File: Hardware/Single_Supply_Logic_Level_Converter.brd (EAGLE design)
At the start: 27.9 x 27.9 mm, 74 parts, among them U1 TXB0104, U2 TPS61200, U3 ADJ

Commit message: Updated per QC review
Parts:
- R1: value 200k -> (none); device SparkFun-Resistors:0603 -> SparkFun-Resistors:AXIAL-0.3
- R2: value 1.8M -> 22k
- R3: value 1k -> 13k
- R4: value 13k -> 1k
- R5: value 22k -> 1.8M
- R6: value (none) -> 200k; device SparkFun-Resistors:AXIAL-0.3 -> SparkFun-Resistors:0603
- moved R2 18.1 mm to (14.0, 1.27)
- moved R1 17.4 mm to (14.0, 1.27), turned to 180 degrees
- moved R5 15.7 mm to (19.4, 17.3)
- moved R6 14.9 mm to (16.0, 17.3), turned to 0 degrees
- moved R3 11.3 mm to (8.29, 5.00), turned to 270 degrees
- moved R4 11.3 mm to (19.5, 5.00), turned to 90 degrees
- moved C3 1.27 mm to (18.9, 21.0)
- moved L1 1.27 mm to (12.0, 25.4)
- moved U$18 1.27 mm to (21.7, 19.1)
- moved U$46 1.27 mm to (19.4, 17.0)
- moved C1 1.27 mm to (9.37, 15.2)
- moved C2 1.27 mm to (18.6, 15.2)
- moved LOGO2 1.27 mm to (14.5, 6.97)
- moved U$31 1.27 mm to (2.46, 6.35)
- moved U$41 1.27 mm to (5.05, 6.35)
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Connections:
- net 5V: now also R5.2; no longer R2.2
- net FB: now also R5.1, R6.2; no longer R1.2, R2.1
- net GND: now also R2.1, R6.1; no longer R1.1, R5.1
- net N$11: now also R1.P$1, R2.2, R3.1; no longer R4.1, R5.2, R6.P$1
- net N$3: now also R4.1; no longer R3.1
- net VCCA: now also R1.P$2; no longer R6.P$2

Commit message: adding PROD ID prefix to 1.8M
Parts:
- moved LOGO2 0.53 mm to (13.9, 7.00)
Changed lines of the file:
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@@
 <attribute name="PROD_ID" value="CAP-00810" x="24.60625" y="-8.89" size="1.778" layer="27" display="off"/>
 </element>
-<element name="LOGO2" library="SparkFun-Aesthetics" package="OSHW-LOGO-S" value="OSHW-LOGOS" x="14.478" y="6.9723" rot="MR0"/>
+<element name="LOGO2" library="SparkFun-Aesthetics" package="OSHW-LOGO-S" value="OSHW-LOGOS" x="13.9446" y="6.9977" rot="MR0"/>
 <element name="C2" library="SparkFun-Capacitors" package="0603-CAP" value="0.1uF" x="18.57375" y="15.24" rot="R180">
 <attribute name="PROD_ID" value="CAP-00810" x="-0.47625" y="39.37" size="1.778" layer="27" rot="R180" display="off"/>
@@
 </element>
 <element name="R5" library="SparkFun-Resistors" package="0603" value="1.8M" x="19.3675" y="17.30375">
-<attribute name="PROD_ID" value="13994" x="19.3675" y="17.30375" size="1.778" layer="27" display="off"/>
+<attribute name="PROD_ID" value="RES-13994" x="19.3675" y="17.30375" size="1.778" layer="27" display="off"/>
 </element>
 <element name="JP3" library="SparkFun-Connectors" package="1X04" value="455-1750-1-ND" x="26.67" y="24.13" rot="R270">

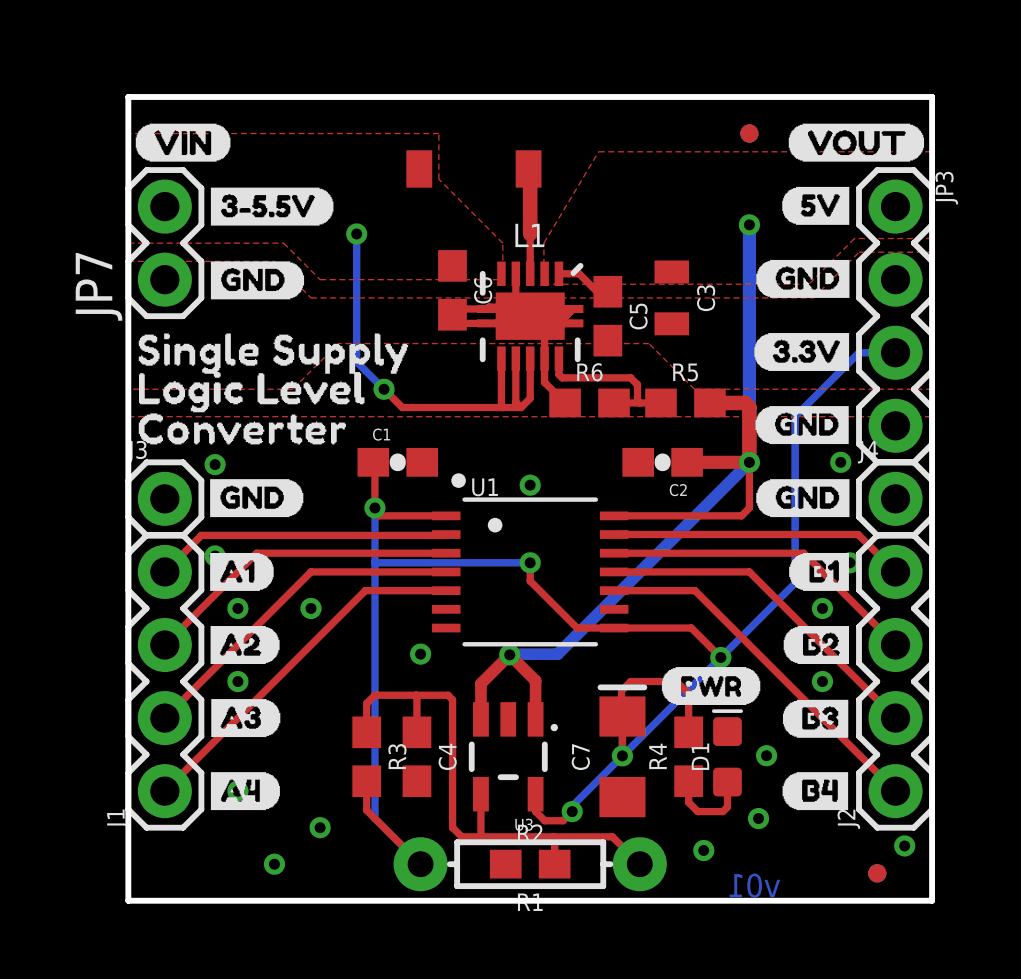
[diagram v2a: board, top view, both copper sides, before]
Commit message: Updated pin labels to SparkX standards
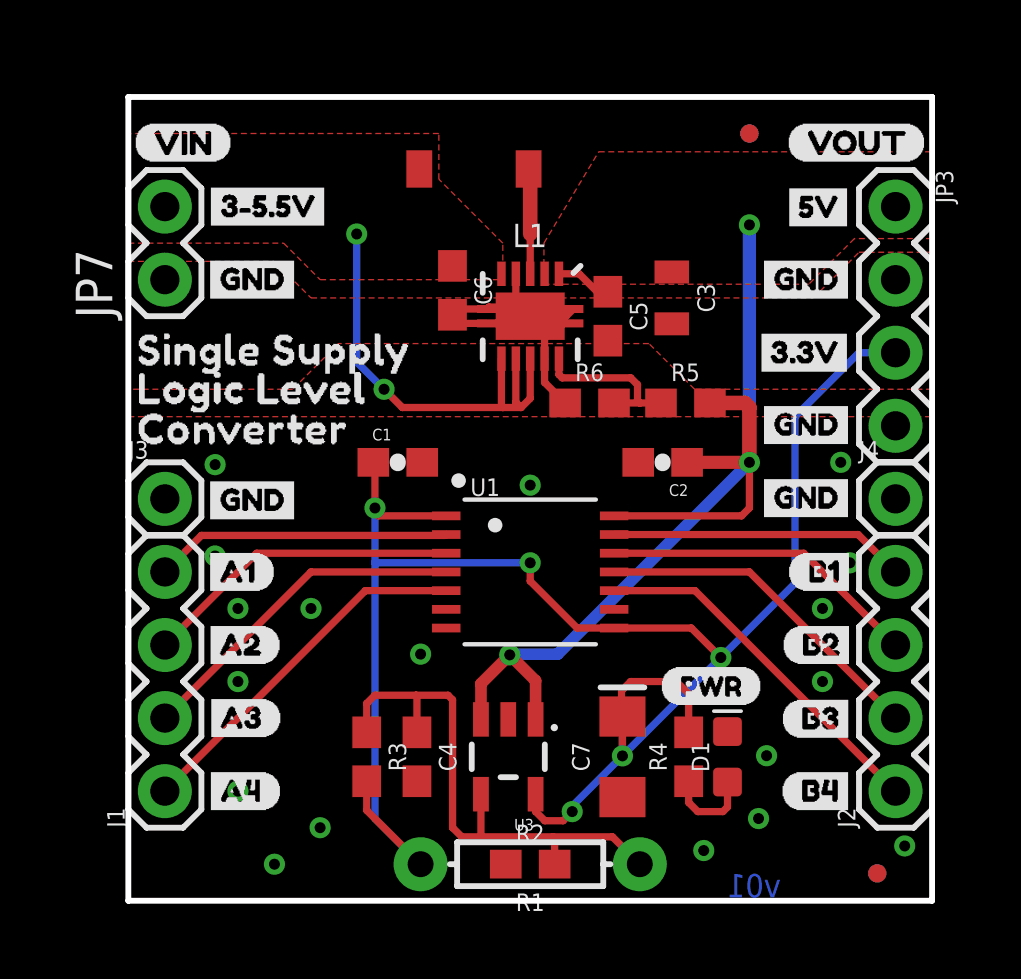
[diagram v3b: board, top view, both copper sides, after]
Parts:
- removed U$36: (no value), buzzard_labels (46):B43
- removed U$38: (no value), buzzard_labels (38):GND3
- removed U$40: (no value), buzzard_labels (38):GND0
- removed U$61: (no value), buzzard_labels (43):B34
- added U$20, U$48: (no value), buzzard_labels (51):3#3V0
- added U$21: (no value), buzzard_labels (51):3#5#5V1
- added U$23, U$47: (no value), buzzard_labels (51):5V3
- added U$44: (no value), buzzard_labels (51):GND2
- U$13, U$24: device buzzard_labels (38):GND3 -> buzzard_labels (51):GND2
- U$14, U$22, U$39, U$9: device buzzard_labels (38):GND0 -> buzzard_labels (51):GND2
- U$15: device buzzard_labels (38):GND3 -> buzzard_labels (43):B13
- U$16: device buzzard_labels (43):3#3V2 -> buzzard_labels (46):B21
- U$17: device buzzard_labels (43):3#5#5V6 -> buzzard_labels (43):B34
- U$18: device buzzard_labels (38):3#3V4 -> buzzard_labels (51):GND2
- U$19: device buzzard_labels (38):5V2 -> buzzard_labels (51):GND2
- U$25: device buzzard_labels (38):GND3 -> buzzard_labels (51):3#5#5V1
- U$33: device buzzard_labels (43):5V10 -> buzzard_labels (46):B43
- U$7: device buzzard_labels (38):3#5#5V1 -> buzzard_labels (51):GND2
- moved U$17 26.0 mm to (25.8, 6.35)
- moved U$9 23.3 mm to (25.8, 21.6), flipped to the bottom
- moved U$15 22.4 mm to (25.8, 11.4)
- moved U$33 20.3 mm to (25.8, 3.81)
- moved U$39 19.6 mm to (5.84, 14.0)
- moved U$24 19.3 mm to (2.46, 13.9)
- moved U$22 19.3 mm to (21.7, 14.0)
- moved U$25 16.7 mm to (6.86, 24.1), flipped to the bottom
- moved U$16 10.2 mm to (25.8, 8.89)
- moved U$19 7.67 mm to (21.7, 16.5)
- moved U$14 7.63 mm to (25.8, 14.0)
- moved U$18 4.85 mm to (25.8, 16.5), flipped to the bottom
- moved U$7 4.21 mm to (5.84, 21.6), flipped to the bottom
- moved U$13 0.06 mm to (21.7, 21.6)

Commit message: increased labels size
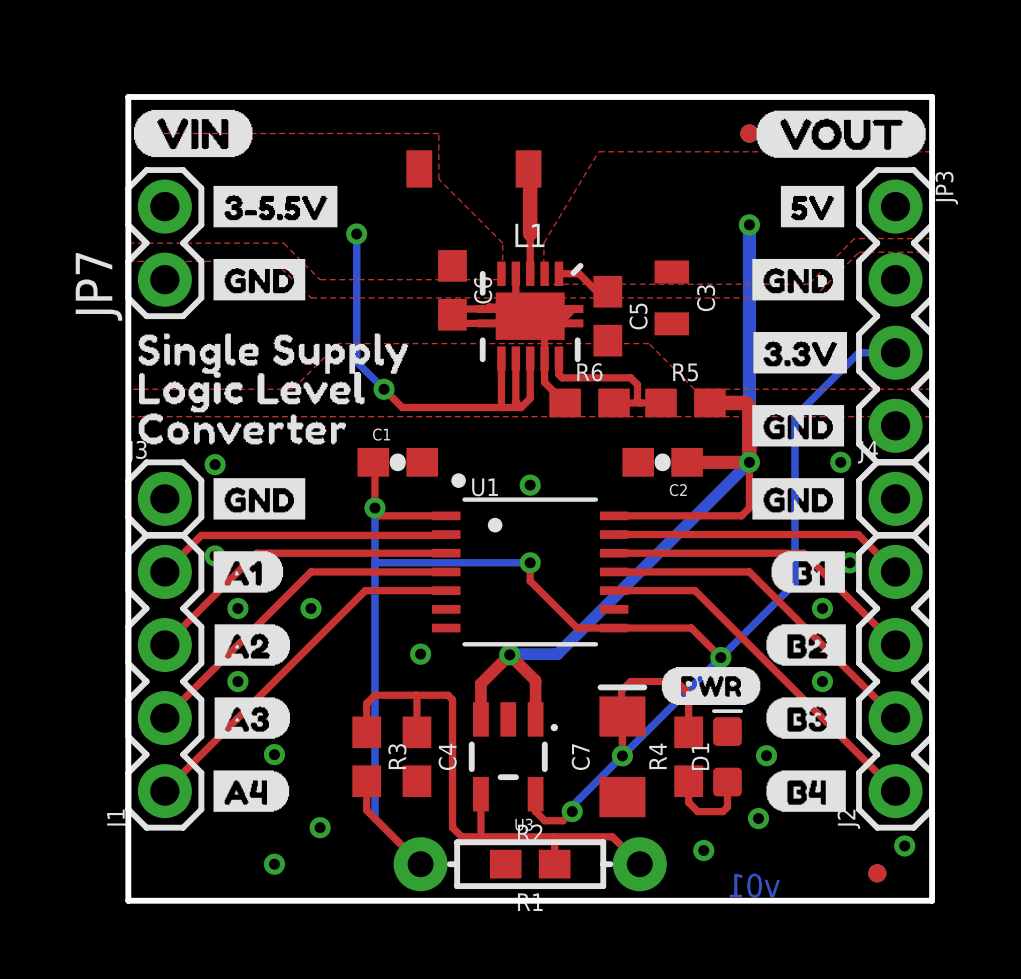
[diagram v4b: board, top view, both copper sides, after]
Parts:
- removed U$37: (no value), buzzard_labels (46):B21
- removed U$44: (no value), buzzard_labels (51):GND2
- removed U$47: (no value), buzzard_labels (51):5V3
- removed U$48: (no value), buzzard_labels (51):3#3V0
- removed U$56: (no value), buzzard_labels (38):B311
- removed U$57: (no value), buzzard_labels (38):B412
- removed U$59: (no value), buzzard_labels (43):B13
- removed U$8: (no value), Single_Supply_Logic_Level_Converter_Lables:VIN1
- added U$36, U$38: (no value), buzzard_labels (84):VIN0
- added U$40: (no value), buzzard_labels (83):GND0
- added U$51: (no value), buzzard_labels (83):5V1
- added U$53: (no value), buzzard_labels (83):3#3V2
- U$13: device buzzard_labels (51):GND2 -> buzzard_labels (83):B1_12
- U$14: device buzzard_labels (51):GND2 -> buzzard_labels (85):A21
- U$15: device buzzard_labels (43):B13 -> buzzard_labels (85):A32
- U$16: device buzzard_labels (46):B21 -> buzzard_labels (85):A43
- U$17: device buzzard_labels (43):B34 -> buzzard_labels (85):B14
- U$18: device buzzard_labels (51):GND2 -> buzzard_labels (85):B25
- U$19: device buzzard_labels (51):GND2 -> buzzard_labels (83):B2_11
- U$20: device buzzard_labels (51):3#3V0 -> buzzard_labels (83):B3_10
- U$21: device buzzard_labels (51):3#5#5V1 -> buzzard_labels (83):3#5#5V3
- U$22: device buzzard_labels (51):GND2 -> buzzard_labels (83):B4_9
- U$23: device buzzard_labels (51):5V3 -> buzzard_labels (83):3#3V2
- U$24, U$7: device buzzard_labels (51):GND2 -> buzzard_labels (83):GND0
- U$25: device buzzard_labels (51):3#5#5V1 -> buzzard_labels (83):A14
- U$26: device buzzard_labels (38):A15 -> buzzard_labels (83):A28
- U$27: device Single_Supply_Logic_Level_Converter_Lables:VIN1 -> buzzard_labels (84):VOUT1
- U$28: device Single_Supply_Logic_Level_Converter_Lables:VOUT2 -> buzzard_labels (83):A35
- U$30: device buzzard_labels (38):A26 -> buzzard_labels (83):A46
- U$31: device buzzard_labels (38):A37 -> buzzard_labels (83):GND0
- U$32: device buzzard_labels (38):A48 -> buzzard_labels (83):5V1
- U$33: device buzzard_labels (46):B43 -> buzzard_labels (85):B36
- U$34: device buzzard_labels (49):A10 -> buzzard_labels (83):GND0
- U$35: device buzzard_labels (49):A21 -> buzzard_labels (83):GND0
- U$39: device buzzard_labels (51):GND2 -> buzzard_labels (83):3#5#5V3
- U$41: device buzzard_labels (49):A32 -> buzzard_labels (83):GND0
- U$42: device buzzard_labels (49):A43 -> buzzard_labels (85):B47
- U$52: device Single_Supply_Logic_Level_Converter_Lables:VOUT2 -> buzzard_labels (83):GND0
- U$54: device buzzard_labels (38):B19 -> buzzard_labels (83):GND0
- U$55: device buzzard_labels (38):B210 -> buzzard_labels (83):GND0
- U$9: device buzzard_labels (51):GND2 -> buzzard_labels (85):A10
- moved U$28 28.5 mm to (2.54, 6.35)
- moved U$32 28.3 mm to (22.2, 24.1)
- moved U$31 24.2 mm to (21.3, 21.6)
- moved U$9 22.6 mm to (5.59, 11.4)
- moved U$27 21.6 mm to (21.7, 26.6)
- moved U$16 20.6 mm to (5.79, 3.84)
- moved U$15 20.6 mm to (5.85, 6.35)
- moved U$14 20.6 mm to (5.85, 8.90)
- moved U$42 20.4 mm to (25.4, 3.81)
- moved U$35 17.9 mm to (21.3, 16.5), flipped to the top
- moved U$34 16.6 mm to (21.3, 14.0), flipped to the top
- moved U$25 13.4 mm to (2.54, 11.4), flipped to the top
- moved U$20 12.7 mm to (22.1, 6.35)
- moved U$39 10.3 mm to (7.68, 24.1)
- moved U$22 10.2 mm to (22.1, 3.81)
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
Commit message: Decreased board width, moved R1/R2 resistors
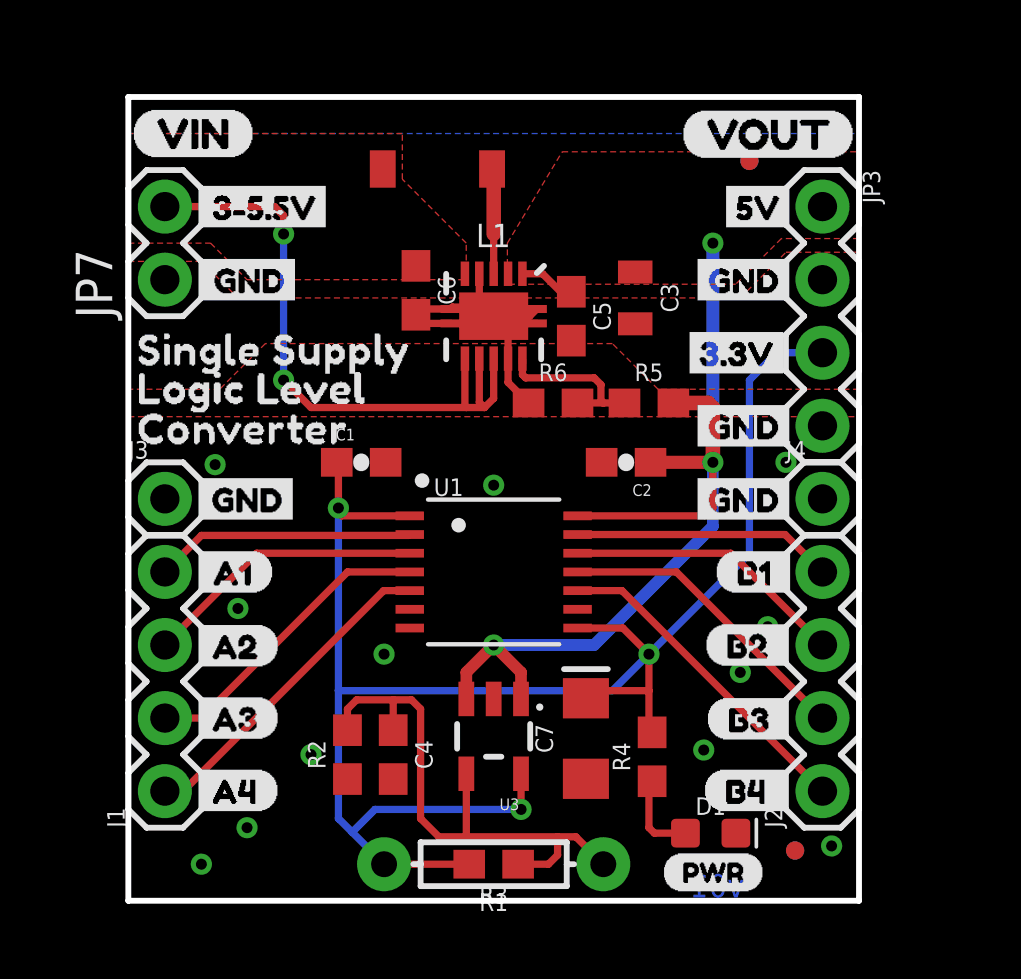
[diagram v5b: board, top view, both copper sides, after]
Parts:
- moved R2 7.41 mm to (7.62, 5.08), turned to 90 degrees
- moved U$29 6.48 mm to (18.5, 0.99)
- moved R3 5.78 mm to (12.7, 1.27), turned to 180 degrees
- moved FD3 2.97 mm to (23.2, 1.75)
- moved FD4 2.97 mm to (23.2, 1.75)
- moved D1 2.72 mm to (20.2, 2.35), turned to 0 degrees
- moved J2 2.54 mm to (24.1, 3.81)
- moved J4 2.54 mm to (24.1, 14.0)
- moved JP3 2.54 mm to (24.1, 24.1)
- moved U$27 2.54 mm to (19.2, 26.6)
- moved U$23 2.22 mm to (19.1, 19.1)
- moved U$22 2.13 mm to (19.9, 3.84)
- moved U$42 2.13 mm to (23.3, 3.81)
- moved U$33 2.11 mm to (23.3, 6.35)
- moved U$51 2.09 mm to (23.3, 24.1)
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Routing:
- net VIN: track 16.1 -> 22.7 mm
- net VCCA: track 66.8 -> 61.4 mm, vias 5 -> 3
- net B1: track 10.3 -> 9.05 mm
- net B4: track 12.7 -> 11.4 mm
- net B3: track 11.9 -> 10.6 mm
- net B2: track 11.1 -> 9.83 mm
- net A3: track 11.9 -> 10.6 mm
- net A4: track 12.7 -> 11.4 mm
- net A2: track 11.1 -> 9.83 mm
- net A1: track 10.3 -> 9.05 mm
- net 5V: track 36.7 -> 35.7 mm
- net GND: vias 18 -> 12
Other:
- board size 27.9 x 27.9 mm -> 25.4 x 27.9 mm
